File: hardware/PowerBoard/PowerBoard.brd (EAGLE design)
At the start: 90 x 56 mm, 136 parts, among them J1 CON-HRS-DM3AT, J2 CON-ZX62R-B-5P, J3 CON-FTSH-105-01-L-DV-K, J4 CON-S2B-PH-SM4-TB, J5 CON-PJ-102A, J6 CON-71436-2164, M1 MOUNT-HOLE3.3, M2 MOUNT-HOLE3.3, M3 MOUNT-HOLE3.3, M4 MOUNT-HOLE3.3, M5 FIDUCIAL1X2, M6 FIDUCIAL1X2, M7 FIDUCIAL1X2, M8 FIDUCIAL1X2, Q1 SI2323CDS, Q2 SI2312CDS, Q3 SI2333CDS, Q4 SI2333CDS, SW1 SWITCH-SPST, SW2 SWITCH-MS12ASG30, U1 LTC4361-2DC, U10 MAX9938FEUK, U11 MAX9938FEUK, U12 MAX9938FEUK, U13 STM32F10XCXT6, U14 LTC2942-1, U15 USBLC6-2, U2 LTC4085, U3 XC6220B331MR-G, U4 XC6220B331MR-G, U5 XC9236A15DMR-G, U6 MIC94043, U7 MAX9938FEUK, U8 MAX9938FEUK, U9 MAX9938FEUK, X1 ECX-2236, X2 ECX-31B

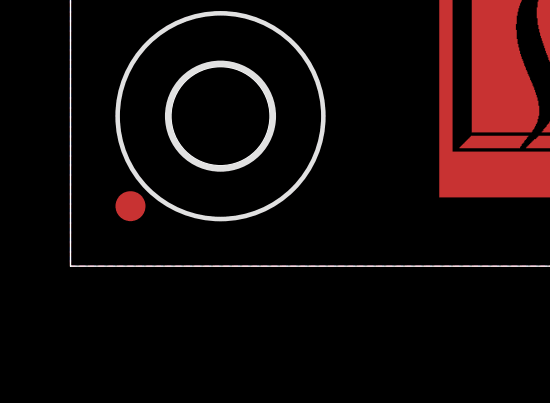
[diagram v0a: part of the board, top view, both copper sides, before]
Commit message: Added USB D+ pull-up resistor and marked possible changes for Rev B.
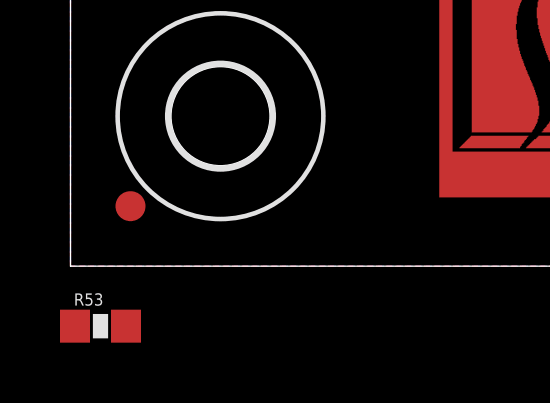
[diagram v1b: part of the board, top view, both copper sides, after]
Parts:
- added R53: 1.5k, powerboard:R0603
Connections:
- net D3V3_STM: now also R53.2
- net USBDP: now also R53.1
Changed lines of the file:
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@@
 <element name="LOGO3" library="Logo" package="LOGO-MARMOTE-10MM-COPPER" value="LOGO-MARMOTE-600MIL-10MM-CU" x="75" y="26.5"/>
 <element name="LOGO4" library="Logo" package="LOGO-BATTERY-10MM-COPPER" value="LOGO-BATTERY-600MIL-10MM-CU" x="75" y="14.25"/>
+<element name="R53" library="powerboard" package="R0603" value="1.5k" x="1" y="-2">
+<attribute name="TOLERANCE" value="" x="1" y="-2" size="1.778" layer="27" display="off"/>
+</element>
 </elements>
 <signals>
@@
 <vertex x="0" y="0"/>
 </polygon>
+<contactref element="R53" pad="2"/>
+<wire x1="34.76" y1="38.76" x2="41.35" y2="38.5" width="0" layer="19" extent="1-16"/>
+<wire x1="27.65" y1="38.5" x2="34.76" y2="38.76" width="0" layer="19" extent="1-16"/>
+<wire x1="30.25" y1="32.75" x2="26.15" y2="36.5" width="0" layer="19" extent="1-16"/>
+<wire x1="21.5" y1="33.25" x2="26.15" y2="36.5" width="0" layer="19" extent="1-16"/>
+<wire x1="26" y1="26" x2="28.75" y2="31" width="0" layer="19" extent="1-16"/>
+<wire x1="27" y1="21.6" x2="25.5" y2="23.75" width="0" layer="19" extent="1-16"/>
+<wire x1="27.85" y1="16.9" x2="29" y2="20.5" width="0" layer="19" extent="16-16"/>
+<wire x1="21.5" y1="23.75" x2="25.5" y2="23.75" width="0" layer="19" extent="1-1"/>
+<wire x1="13.25" y1="36.5" x2="20.25" y2="35.5" width="0" layer="19" extent="1-1"/>
+<wire x1="36" y1="27.55" x2="30.25" y2="31.85" width="0" layer="19" extent="1-1"/>
+<wire x1="39.25" y1="30.6" x2="37.75" y2="27.65" width="0" layer="19" extent="1-16"/>
+<wire x1="11.4" y1="26.5" x2="19.35" y2="25" width="0" layer="19" extent="1-16"/>
+<wire x1="6" y1="20.5" x2="8.1209" y2="27.46" width="0" layer="19" extent="1-1"/>
+<wire x1="10.65" y1="51" x2="13.25" y2="37.65" width="0" layer="19" extent="1-16"/>
+<wire x1="1.85" y1="-2" x2="6" y2="20.5" width="0" layer="19" extent="1-1"/>
 </signal>
 <signal name="I2C2_SDA">
@@
 <via x="23" y="36.5" extent="1-16" drill="0.234"/>
 <via x="23" y="33.75" extent="1-16" drill="0.234"/>
+<contactref element="R53" pad="1"/>
+<wire x1="0.15" y1="-2" x2="23" y2="32.75" width="0" layer="19" extent="1-1"/>
 </signal>
 <signal name="SWDIO">

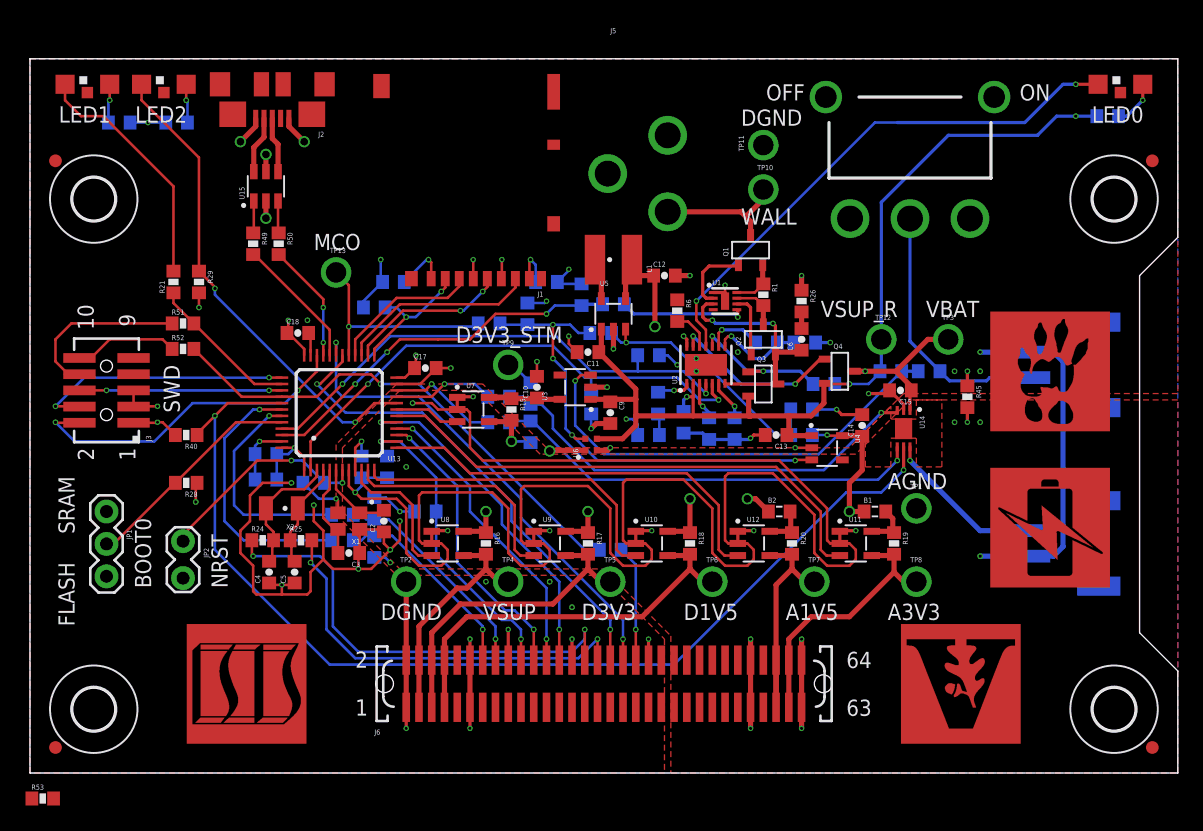
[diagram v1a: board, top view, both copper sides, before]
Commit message: - New 84 board-to-board connector (in schematic and routed) - info text on back corrected
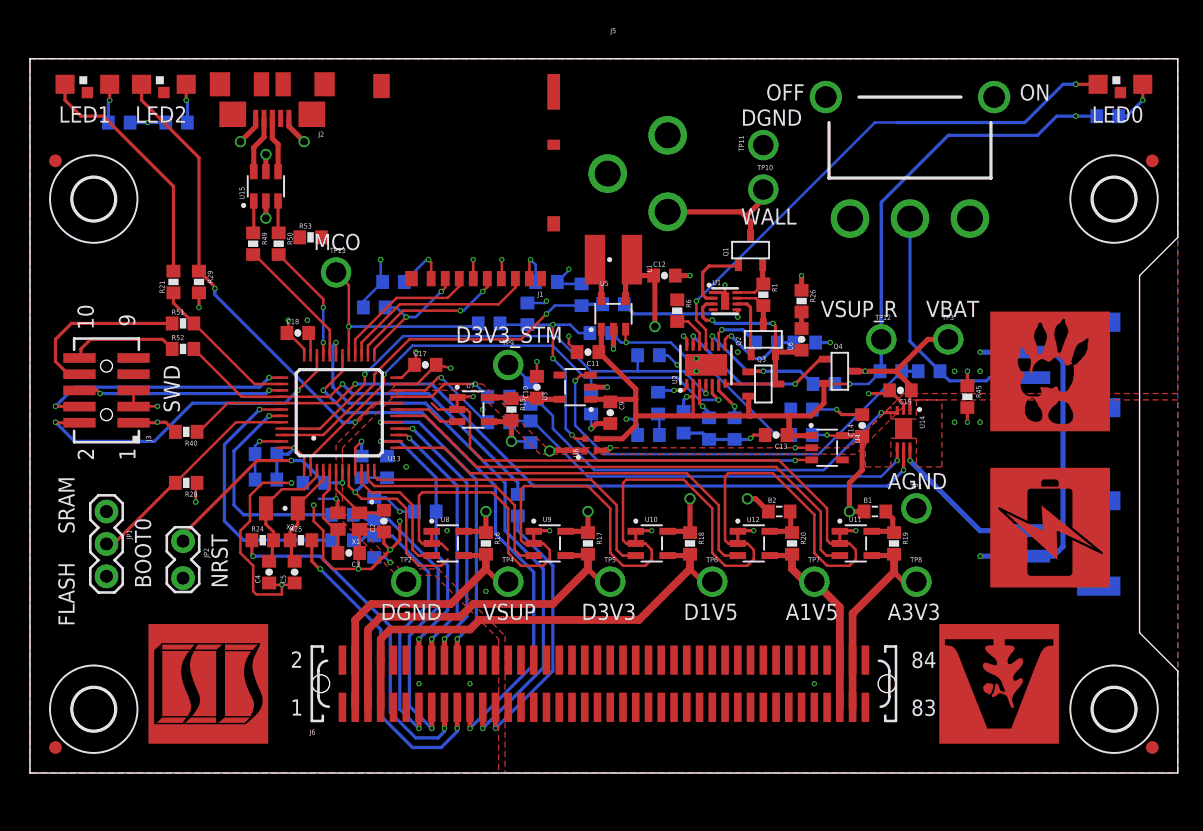
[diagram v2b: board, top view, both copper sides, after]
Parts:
- J6: value CON-71436-2164 -> CON-71741-0002-TOP; device powerboard:71436-XX64 -> powerboard:71741-0002
- moved R53 48.8 mm to (22.0, 42.0)
- moved R48 8.05 mm to (38.2, 21.0), turned to 90 degrees
- moved LOGO1 3.00 mm to (9.00, 2.00)
- moved LOGO2 3.00 mm to (71.0, 2.00)
- moved C17 0.25 mm to (31.0, 32.0)
- moved R40 0.25 mm to (12.2, 26.8)
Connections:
- net A1V5: now also J6.79, J6.80; no longer J6.59, J6.60
- net A3V3: now also J6.81, J6.82; no longer J6.61, J6.62
- net AGND: now also J6.75, J6.76, J6.83, J6.84; no longer J6.55, J6.56, J6.63, J6.64
- net DGND: now also J6.22; no longer J6.18, J6.28, J6.40
- net I2C1_SCL: now also J6.13; no longer J6.14
- net I2C1_SDA: now also J6.15; no longer J6.16
- net PA10: now also J6.23; no longer J6.36
- net PA9: now also J6.21; no longer J6.34
- net PB4-SF: now also J6.25; no longer J6.38
- net PC14: now also J6.17; no longer J6.30
- net PC15: now also J6.19; no longer J6.32
- net SPI1_MISO: now also J6.18; no longer J6.24
- net SPI1_MOSI: now also J6.20; no longer J6.26
- net SPI1_NSS: now also J6.14; no longer J6.20
- net SPI1_SCK: now also J6.16; no longer J6.22
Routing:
- net DGND: track 157.5 -> 126.4 mm, vias 49 -> 42
- net PB5: track 84.1 -> 62.3 mm
- net AGND: track 180.1 -> 162.9 mm, vias 16 -> 14
- net PB4-SF: track 9.13 -> 21.3 mm
- net PC14: track 36.6 -> 28.3 mm
- net PB4: track 39.8 -> 31.5 mm
- net I2C1_SDA: track 17.4 -> 24.2 mm
- net I2C1_SCL: track 15.9 -> 22.7 mm
- net PA10: track 38.7 -> 45.3 mm
- net PC15: track 32.0 -> 25.5 mm
- net PA9: track 37.9 -> 43.9 mm
- net VSUP: track 19.1 -> 24.4 mm
- net D3V3: track 25.3 -> 30.4 mm
- net D1V5: track 32.0 -> 37.0 mm
- net A3V3: track 21.0 -> 17.3 mm
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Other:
- board text added: "Copyright c 2012"
- board text added: "Vanderbilt University, ISIS"
- board text removed: "Copyright © 2012 Vanderbilt University, ISIS"

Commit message: - Schematic updated
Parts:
- moved R53 0.71 mm to (21.5, 41.5), turned to 90 degrees
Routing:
- net AGND: track 162.9 -> 18.0 mm
- net USBDP: track 9.35 -> 11.3 mm
- net D3V3_STM: track 48.0 -> 48.5 mm, vias 13 -> 14

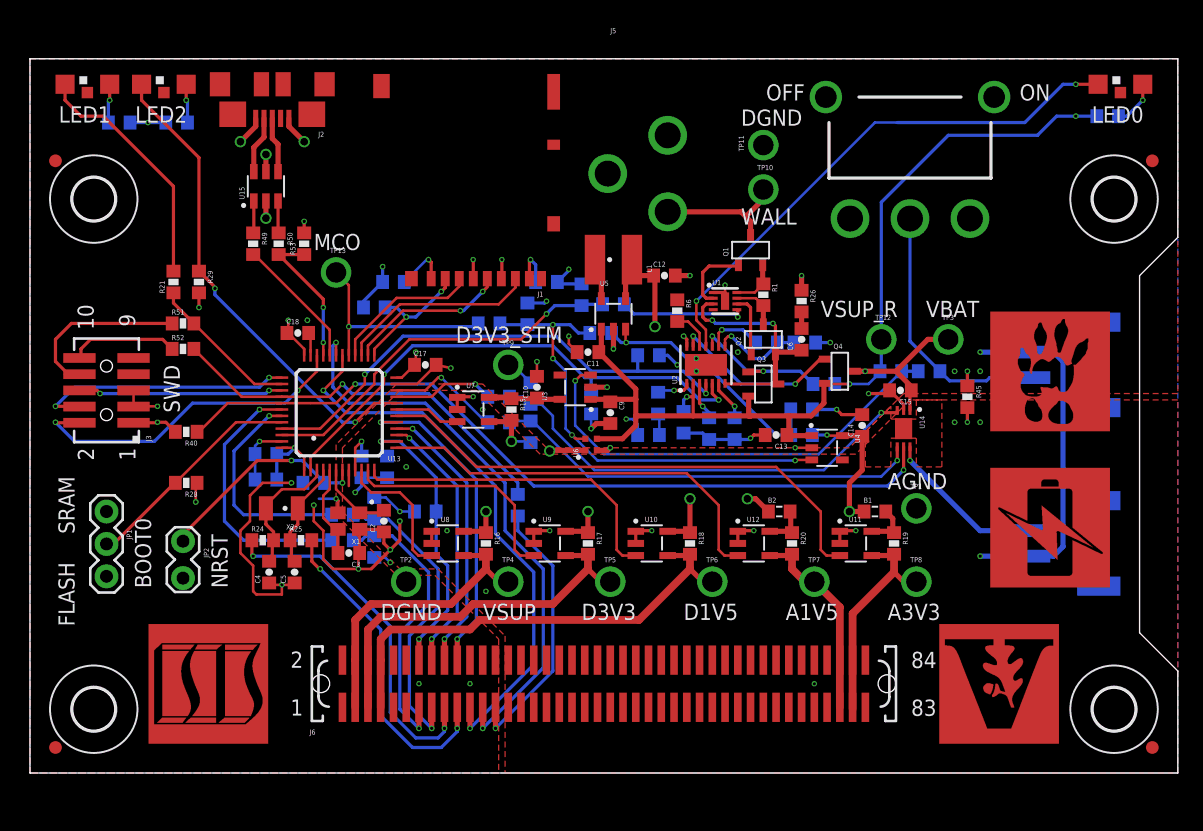
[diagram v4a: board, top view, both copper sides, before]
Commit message: - Logos changed - Small vias covered
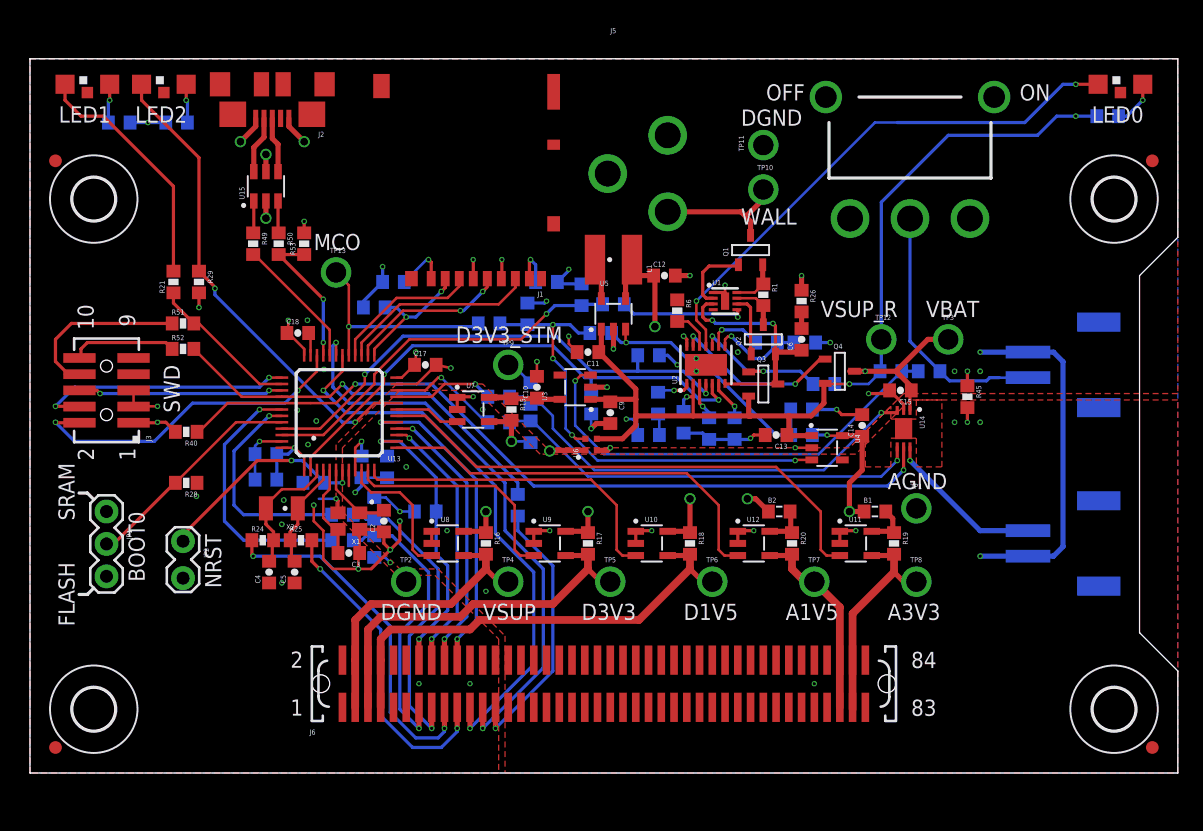
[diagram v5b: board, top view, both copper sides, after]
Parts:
- removed LOGO2: LOGO-VANDERBILT-600MIL-10MM-CU, Logo:LOGO-VANDERBILT-10MM-COPPER
- removed LOGO3: LOGO-MARMOTE-600MIL-10MM-CU, Logo:LOGO-MARMOTE-10MM-COPPER
- removed LOGO4: LOGO-BATTERY-600MIL-10MM-CU, Logo:LOGO-BATTERY-10MM-COPPER
- added LOGO5: LOGO-VANDERBILT-600MIL-10MM-AU, Logo:LOGO-VANDERBILT-10MM-GOLD
- added LOGO6: LOGO-ISIS-600MIL-10MM-AU, Logo:LOGO-ISIS-10MM-GOLD
- added LOGO7: LOGO-MARMOTE-600MIL-10MM-AU, Logo:LOGO-MARMOTE-10MM-GOLD
- LOGO1: value LOGO-ISIS-600MIL-10MM-CU -> LOGO-BATTERY-600MIL-10MM-AU; device Logo:LOGO-ISIS-10MM-COPPER -> Logo:LOGO-BATTERY-10MM-GOLD
- moved LOGO1 67.1 mm to (75.0, 14.2)
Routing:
- net DGND: track 126.4 -> 108.3 mm, vias 42 -> 47

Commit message: - Supply voltage measurement changes - PB9 monitors /CHRG (no led)
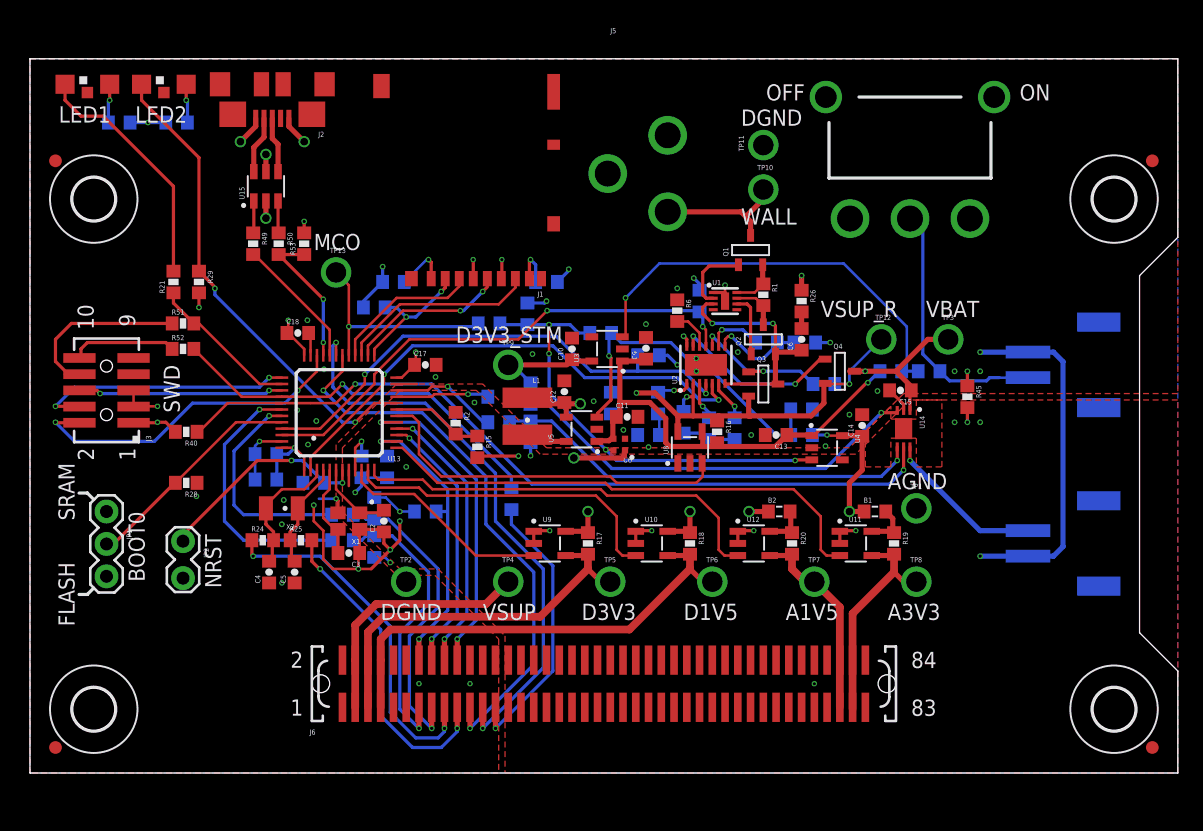
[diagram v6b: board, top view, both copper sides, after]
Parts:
- removed LED0: ORANGE, powerboard:LED1208-RA
- removed R3: 10k, powerboard:R0603
- removed U7: MAX9938FEUK, powerboard:SOT23-5L
- R15: value 50m -> 100k
- R2: value 1k -> 100k
- R5: value 510 -> 10k
- moved R5 35.1 mm to (52.5, 37.0), turned to 90 degrees
- moved U8 20.4 mm to (51.8, 25.5), turned to 90 degrees
- moved R16 20.1 mm to (53.9, 26.8)
- moved R2 15.5 mm to (33.4, 27.4), flipped to the top, turned to 270 degrees
- moved L1 14.0 mm to (39.0, 28.0), turned to 180 degrees
- moved C12 12.0 mm to (41.9, 29.9), turned to 90 degrees
- moved U5 9.39 mm to (43.2, 26.9), turned to 90 degrees
- moved C11 5.93 mm to (46.8, 27.9), turned to 0 degrees
- moved C9 5.77 mm to (48.3, 33.3), turned to 90 degrees
- moved C10 4.07 mm to (42.5, 33.2)
- moved R15 3.96 mm to (35.1, 25.6)
- moved U3 3.91 mm to (45.2, 33.2)
- moved U6 2.20 mm to (46.2, 25.8), turned to 180 degrees
- moved R43 1.55 mm to (45.5, 29.0)
- moved R48 0.71 mm to (37.8, 21.5)
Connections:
- removed net !CHRG: LED0.1, U2.11
- removed net !PWRGD: R2.2, U1.5
- removed net D3V3_STM_I: C10.1, R15.1, U3.5, U7.5
- removed net D3V3_STM_SENSE: U13.19, U7.3
- removed net N$8: LED0.2, R5.1
- removed net VSUP_SENSE: U13.10, U8.3
- new net VSUP_I_SENSE: U13.18, U8.3
- new net VSUP_V_SENSE: R15.1, R2.2, U13.19
- net A1V5_SENSE: now also U13.12; no longer U13.13
- net A3V3_SENSE: now also U13.13; no longer U13.18
- net AGND: now also R2.1; no longer U7.1, U7.2
- net D1V5_SENSE: now also U13.11; no longer U13.12
- net D3V3_SENSE: now also U13.10; no longer U13.11
- net D3V3_STM: now also C10.1, R5.2, U3.5; no longer R15.2, R3.2, U7.4
- net PB9: now also R5.1, U2.11; no longer R2.1, R3.1
- net VSUP: now also U6.1; no longer R16.2, U8.4
- net VSUP_I: now also C11.1, C13.1, C9.1, R10.1, R16.2, U3.1, U4.1, U5.1, U6.3, U8.4; no longer R16.1, U6.1, U8.5
- net VSUP_R: now also R15.2, R16.1, U8.5; no longer C11.1, C13.1, C9.1, R10.1, R5.2, U3.1, U4.1, U5.1, U6.3
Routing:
- net !CHRG: track 42.4 -> 0.00 mm, vias 2 -> 0
- net VSUP_R: track 81.7 -> 47.7 mm, vias 3 -> 4
- net VSUP_I_SENSE: track 0.00 -> 28.9 mm
- net DGND: track 108.3 -> 83.2 mm, vias 47 -> 45
- net VSUP_I: track 13.2 -> 34.0 mm, vias 2 -> 1
- net VSUP: track 24.4 -> 36.0 mm, vias 0 -> 1
- net VSUP_SENSE: track 10.9 -> 0.00 mm
- net PB9: track 29.8 -> 39.9 mm, vias 1 -> 2
- net !PWRGD: track 9.92 -> 0.00 mm, vias 1 -> 0
- net D1V5_I: track 36.0 -> 28.1 mm
- net VSUP_V_SENSE: track 0.00 -> 6.42 mm
- net D1V5-EN: track 20.4 -> 26.4 mm
- net D3V3_STM_I: track 5.65 -> 0.00 mm
- net D3V3_STM_SENSE: track 5.14 -> 0.00 mm
- net N$8: track 3.67 -> 0.00 mm, vias 1 -> 0
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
